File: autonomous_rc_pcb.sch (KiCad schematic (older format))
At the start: 19 parts, among them P1 USB_A_Vertical, P2 HDMI_PAUL, P7 USB_A_Vertical, U5 ESD-8040

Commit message: beta
beta pcb version 0.001V
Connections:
- net +12C: no longer ETHERNET1.6 (POE_VCC)
- net +28V: no longer POWER1.1 (Pin_1)
- new net +12V: ETHERNET1.6 (POE_VCC)
- new net +36V: POWER1.1 (Pin_1)
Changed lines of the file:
@@
-	1    0    0    -1
-$EndComp
-$Comp
-L +28V #PWR015
-U 1 1 5AF6179F
-P 1200 1350
-F 0 "#PWR015" H 1200 1200 50  0001 C CNN
-F 1 "+28V" H 1200 1500 50  0000 C CNN
-F 2 "" H 1450 1400 50  0001 C CNN
-F 3 "" H 1450 1400 50  0001 C CNN
-	1    1200 1350
 	1    0    0    -1
 $EndComp
@@
 	1    0    0    -1
 $EndComp
-$Comp
-L +12C #PWR039
-U 1 1 5B01DB59
-P 11550 6200
-F 0 "#PWR039" H 11550 6050 50  0001 C CNN
-F 1 "+12C" H 11550 6350 50  0000 C CNN
-F 2 "" H 11550 6200 50  0001 C CNN
-F 3 "" H 11550 6200 50  0001 C CNN
-	1    11550 6200
-	1    0    0    -1
-$EndComp
 NoConn ~ 11350 6150
 NoConn ~ 11350 6250
@@
 USB_ETHER+
 $Comp
-L GND #PWR040
+L GND #PWR039
 U 1 1 5B03A700
 P 10050 7450
-F 0 "#PWR040" H 10050 7200 50  0001 C CNN
+F 0 "#PWR039" H 10050 7200 50  0001 C CNN
 F 1 "GND" H 10050 7300 50  0000 C CNN
 F 2 "" H 10050 7450 50  0001 C CNN
@@
 $EndComp
 $Comp
-L GND #PWR041
+L GND #PWR040
 U 1 1 5B03A9DA
 P 10200 7450
-F 0 "#PWR041" H 10200 7200 50  0001 C CNN
+F 0 "#PWR040" H 10200 7200 50  0001 C CNN
 F 1 "GND" H 10200 7300 50  0000 C CNN
 F 2 "" H 10200 7450 50  0001 C CNN
@@
 Connection ~ 11850 3450
 Connection ~ 13050 3450
+$Comp
+L +12V #PWR041
+U 1 1 5B054AB8
+P 11550 6200
+F 0 "#PWR041" H 11550 6050 50  0001 C CNN
+F 1 "+12V" H 11550 6340 50  0000 C CNN
+F 2 "" H 11550 6200 50  0001 C CNN
+F 3 "" H 11550 6200 50  0001 C CNN
+	1    11550 6200
+	1    0    0    -1
+$EndComp
+$Comp
+L +36V #PWR?
+U 1 1 5B06C817
+P 1200 1350
+F 0 "#PWR?" H 1200 1200 50  0001 C CNN
+F 1 "+36V" H 1200 1490 50  0000 C CNN
+F 2 "" H 1200 1350 50  0001 C CNN
+F 3 "" H 1200 1350 50  0001 C CNN
+	1    1200 1350
+	1    0    0    -1
+$EndComp
 $EndSCHEMATC

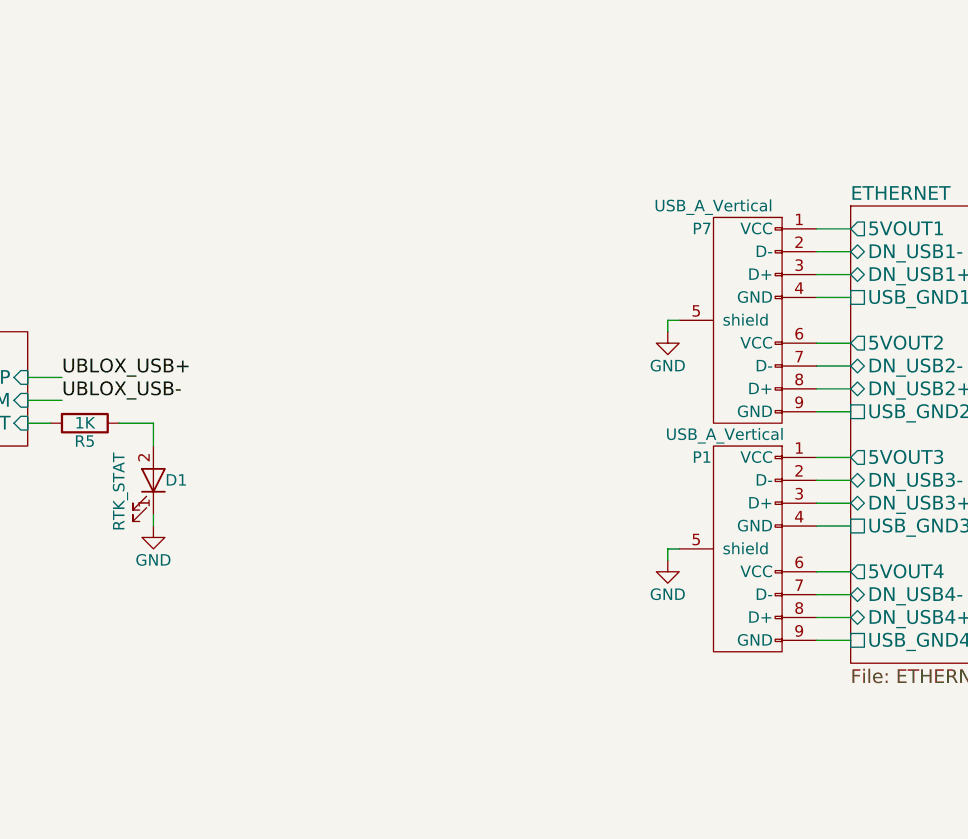
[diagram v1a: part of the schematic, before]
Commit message: tuned rf
added u.fl connectors to tune line 
moved some lines under rf components
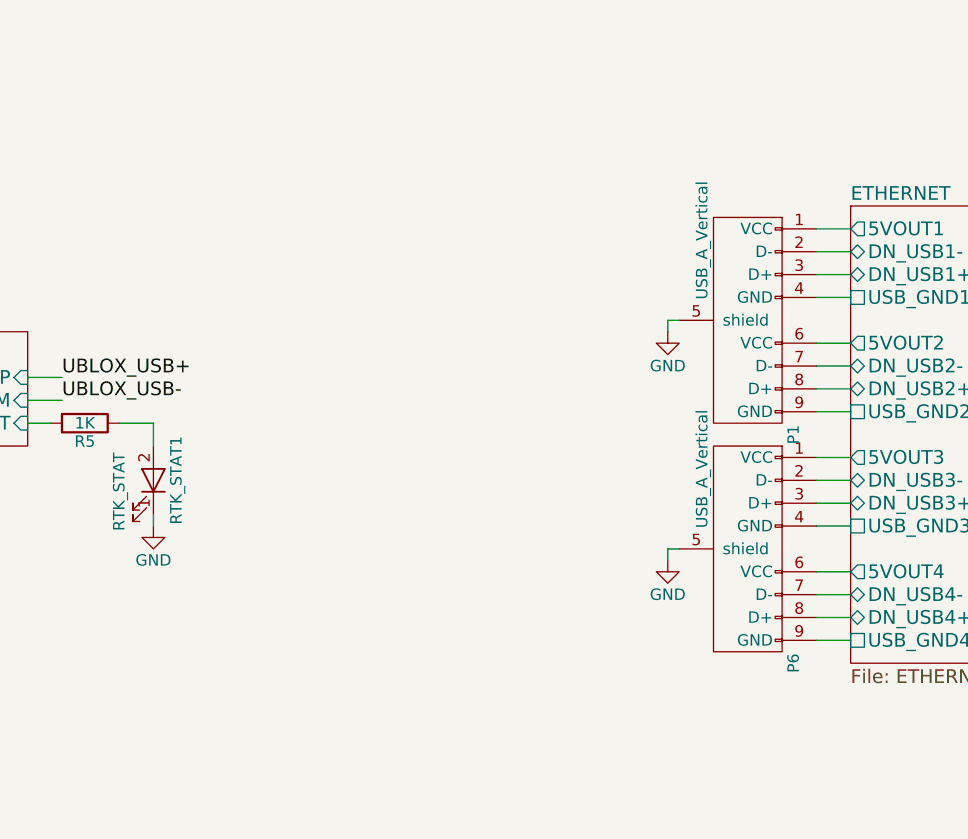
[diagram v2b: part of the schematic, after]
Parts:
- removed P7: USB_A_Vertical, Don-Con:USB_A_Stacked, symbol USB_A_Vertical
- added P6: USB_A_Vertical, Don-Con:USB-A-vertical, symbol USB_A_Vertical
- P1: footprint Don-Con:USB_A_Stacked -> Don-Con:USB-A-vertical
- renumbered D1 to RTK_STAT1
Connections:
- net ETHERNET/5VOUT1: now also P1.1 (VCC)
- net ETHERNET/5VOUT2: now also P1.6 (VCC)
- net ETHERNET/5VOUT3: now also P6.1 (VCC); no longer P1.1 (VCC)
- net ETHERNET/5VOUT4: now also P6.6 (VCC); no longer P1.6 (VCC)
- net ETHERNET/DN_USB1+: now also P1.3 (D+)
- net ETHERNET/DN_USB1-: now also P1.2 (D-)
- net ETHERNET/DN_USB2+: now also P1.8 (D+)
- net ETHERNET/DN_USB2-: now also P1.7 (D-)
- net ETHERNET/DN_USB3+: now also P6.3 (D+); no longer P1.3 (D+)
- net ETHERNET/DN_USB3-: now also P6.2 (D-); no longer P1.2 (D-)
- net ETHERNET/DN_USB4+: now also P6.8 (D+); no longer P1.8 (D+)
- net ETHERNET/DN_USB4-: now also P6.7 (D-); no longer P1.7 (D-)
- net ETHERNET/USB_GND1: now also P1.4 (GND)
- net ETHERNET/USB_GND2: now also P1.9 (GND)
- net ETHERNET/USB_GND3: now also P6.4 (GND); no longer P1.4 (GND)
- net ETHERNET/USB_GND4: now also P6.9 (GND); no longer P1.9 (GND)
- net GND: now also P6.5 (shield)
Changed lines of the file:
@@
 $EndSheet
 $Comp
-L LED D1
+L LED RTK_STAT1
 U 1 1 5AF2A043
 P 5300 6250
-F 0 "D1" V 5300 6350 50  0000 C CNN
+F 0 "RTK_STAT1" H 5300 6350 50  0000 C CNN
 F 1 "RTK_STAT" H 5250 6100 50  0000 C CNN
 F 2 "LEDs:LED_0603" H 5300 6250 50  0001 C CNN
@@
 STM_USB_N
 $Comp
-L +28V #PWR016
+L +28V #PWR015
 U 1 1 5AF68A51
 P 3100 900
-F 0 "#PWR016" H 3100 750 50  0001 C CNN
+F 0 "#PWR015" H 3100 750 50  0001 C CNN
 F 1 "+28V" H 3100 1050 50  0000 C CNN
 F 2 "" H 3350 950 50  0001 C CNN
@@
 $EndComp
 $Comp
-L +3V3 #PWR017
+L +3V3 #PWR016
 U 1 1 5AF68C87
 P 3900 900
-F 0 "#PWR017" H 3900 750 50  0001 C CNN
+F 0 "#PWR016" H 3900 750 50  0001 C CNN
 F 1 "+3V3" H 3900 1040 50  0000 C CNN
 F 2 "" H 3900 900 50  0001 C CNN
@@
 $EndComp
 $Comp
-L +1V8 #PWR018
+L +1V8 #PWR017
 U 1 1 5AF68EBD
 P 4300 900
-F 0 "#PWR018" H 4300 750 50  0001 C CNN
+F 0 "#PWR017" H 4300 750 50  0001 C CNN
 F 1 "+1V8" H 4300 1040 50  0000 C CNN
 F 2 "" H 4300 900 50  0001 C CNN
@@
 $EndComp
 $Comp
-L +5V #PWR019
+L +5V #PWR018
 U 1 1 5AF690F3
 P 4700 900
-F 0 "#PWR019" H 4700 750 50  0001 C CNN
+F 0 "#PWR018" H 4700 750 50  0001 C CNN
 F 1 "+5V" H 4700 1040 50  0000 C CNN
 F 2 "" H 4700 900 50  0001 C CNN
@@
 $EndComp
 $Comp
-L GND #PWR020
+L GND #PWR019
 U 1 1 5AF69329
 P 5000 1150
-F 0 "#PWR020" H 5000 900 50  0001 C CNN
+F 0 "#PWR019" H 5000 900 50  0001 C CNN
 F 1 "GND" H 5000 1000 50  0000 C CNN
 F 2 "" H 5000 1150 50  0001 C CNN
@@
 $EndComp
 $Comp
-L PWR_FLAG #FLG021
+L PWR_FLAG #FLG020
 U 1 1 5AF6955F
 P 5000 900
-F 0 "#FLG021" H 5000 975 50  0001 C CNN
+F 0 "#FLG020" H 5000 975 50  0001 C CNN
 F 1 "PWR_FLAG" H 5000 1050 50  0000 C CNN
 F 2 "" H 5000 900 50  0001 C CNN
@@
 $EndComp
 $Comp
-L PWR_FLAG #FLG022
+L PWR_FLAG #FLG021
 U 1 1 5AF69795
 P 3100 1150
-F 0 "#FLG022" H 3100 1225 50  0001 C CNN
+F 0 "#FLG021" H 3100 1225 50  0001 C CNN
 F 1 "PWR_FLAG" H 3100 1300 50  0000 C CNN
 F 2 "" H 3100 1150 50  0001 C CNN
@@
 $EndComp
 $Comp
-L PWR_FLAG #FLG023
+L PWR_FLAG #FLG022
 U 1 1 5AF69BF4
 P 3900 1150
-F 0 "#FLG023" H 3900 1225 50  0001 C CNN
+F 0 "#FLG022" H 3900 1225 50  0001 C CNN
 F 1 "PWR_FLAG" H 3900 1300 50  0000 C CNN
 F 2 "" H 3900 1150 50  0001 C CNN
@@
 $EndComp
 $Comp
-L PWR_FLAG #FLG024
+L PWR_FLAG #FLG023
 U 1 1 5AF69E2A
 P 4300 1150
-F 0 "#FLG024" H 4300 1225 50  0001 C CNN
+F 0 "#FLG023" H 4300 1225 50  0001 C CNN
 F 1 "PWR_FLAG" H 4300 1300 50  0000 C CNN
 F 2 "" H 4300 1150 50  0001 C CNN
@@
 $EndComp
 $Comp
-L PWR_FLAG #FLG025
+L PWR_FLAG #FLG024
 U 1 1 5AF6A060
 P 4700 1150
-F 0 "#FLG025" H 4700 1225 50  0001 C CNN
+F 0 "#FLG024" H 4700 1225 50  0001 C CNN
 F 1 "PWR_FLAG" H 4700 1300 50  0000 C CNN
 F 2 "" H 4700 1150 50  0001 C CNN
@@
 NoConn ~ 11850 3250
 $Comp
-L +5V #PWR026
+L +5V #PWR025
 U 1 1 5AF9117D
 P 13200 3650
-F 0 "#PWR026" H 13200 3500 50  0001 C CNN
+F 0 "#PWR025" H 13200 3500 50  0001 C CNN
 F 1 "+5V" H 13200 3790 50  0000 C CNN
 F 2 "" H 13200 3650 50  0001 C CNN
@@
 UBLOX_USB-
 $Comp
-L +5V #PWR027
+L +5V #PWR026
 U 1 1 5AFDF0D4
 P 1500 7350
-F 0 "#PWR027" H 1500 7200 50  0001 C CNN
+F 0 "#PWR026" H 1500 7200 50  0001 C CNN
 F 1 "+5V" H 1500 7490 50  0000 C CNN
 F 2 "" H 1500 7350 50  0001 C CNN
@@
 $EndComp
 $Comp
-L GND #PWR028
+L GND #PWR027
 U 1 1 5AFDF0DA
 P 1650 7650
-F 0 "#PWR028" H 1650 7400 50  0001 C CNN
+F 0 "#PWR027" H 1650 7400 50  0001 C CNN
 F 1 "GND" H 1650 7500 50  0000 C CNN
 F 2 "" H 1650 7650 50  0001 C CNN
@@
 $EndComp
 $Comp
-L +5V #PWR029
+L +5V #PWR028
 U 1 1 5AFDF99D
 P 1500 8000
-F 0 "#PWR029" H 1500 7850 50  0001 C CNN
+F 0 "#PWR028" H 1500 7850 50  0001 C CNN
 F 1 "+5V" H 1500 8140 50  0000 C CNN
 F 2 "" H 1500 8000 50  0001 C CNN
@@
 $EndComp
 $Comp
-L GND #PWR030
+L GND #PWR029
 U 1 1 5AFDF9A3
 P 1650 8300
-F 0 "#PWR030" H 1650 8050 50  0001 C CNN
+F 0 "#PWR029" H 1650 8050 50  0001 C CNN
 F 1 "GND" H 1650 8150 50  0000 C CNN
 F 2 "" H 1650 8300 50  0001 C CNN
@@
 $EndComp
 $Comp
-L +5V #PWR031
+L +5V #PWR030
 U 1 1 5AFDFFC7
 P 1500 8650
-F 0 "#PWR031" H 1500 8500 50  0001 C CNN
+F 0 "#PWR030" H 1500 8500 50  0001 C CNN
 F 1 "+5V" H 1500 8790 50  0000 C CNN
 F 2 "" H 1500 8650 50  0001 C CNN
@@
 $EndComp
 $Comp
-L GND #PWR032
+L GND #PWR031
 U 1 1 5AFDFFCD
 P 1650 8950
-F 0 "#PWR032" H 1650 8700 50  0001 C CNN
+F 0 "#PWR031" H 1650 8700 50  0001 C CNN
 F 1 "GND" H 1650 8800 50  0000 C CNN
 F 2 "" H 1650 8950 50  0001 C CNN
@@
 VBAT_ADC
 $Comp
-L PWR_FLAG #FLG033
+L PWR_FLAG #FLG032
 U 1 1 5B0318FE
 P 3500 1150
-F 0 "#FLG033" H 3500 1225 50  0001 C CNN
+F 0 "#FLG032" H 3500 1225 50  0001 C CNN
 F 1 "PWR_FLAG" H 3500 1300 50  0000 C CNN
 F 2 "" H 3500 1150 50  0001 C CNN
@@
 $EndComp
 $Comp
-L +12C #PWR034
+L +12C #PWR033
 U 1 1 5B031F00
 P 3500 900
-F 0 "#PWR034" H 3500 750 50  0001 C CNN
+F 0 "#PWR033" H 3500 750 50  0001 C CNN
 F 1 "+12C" H 3500 1050 50  0000 C CNN
 F 2 "" H 3500 900 50  0001 C CNN
@@
 UBLOX_USB-
 $Comp
-L GND #PWR035
+L GND #PWR034
 U 1 1 5AFCCFA1
 P 7550 5600
-F 0 "#PWR035" H 7550 5350 50  0001 C CNN
+F 0 "#PWR034" H 7550 5350 50  0001 C CNN
 F 1 "GND" H 7550 5450 50  0000 C CNN
 F 2 "" H 7550 5600 50  0001 C CNN
 F 3 "" H 7550 5600 50  0001 C CNN
 	1    7550 5600
-	1    0    0    -1
-$EndComp
-$Comp
-L USB_A_Vertical P7
-U 1 1 5AFCCF9B
-P 8000 5550
-F 0 "P7" H 7700 5950 50  0000 C CNN
-F 1 "USB_A_Vertical" H 7750 6050 50  0000 C CNN
-F 2 "Don-Con:USB_A_Stacked" H 8000 5300 60  0001 C CNN
-F 3 "" H 8000 5300 60  0000 C CNN
-	1    8000 5550
 	1    0    0    -1
 $EndComp
@@
 $EndSheet
 $Comp
-L GND #PWR036
+L GND #PWR035
 U 1 1 5B006ACE
 P 7550 6600
-F 0 "#PWR036" H 7550 6350 50  0001 C CNN
+F 0 "#PWR035" H 7550 6350 50  0001 C CNN
 F 1 "GND" H 7550 6450 50  0000 C CNN
 F 2 "" H 7550 6600 50  0001 C CNN
 F 3 "" H 7550 6600 50  0001 C CNN
 	1    7550 6600
-	1    0    0    -1
-$EndComp
-$Comp
-L USB_A_Vertical P1
-U 1 1 5B006AD4
-P 8000 6550
-F 0 "P1" H 7700 6950 50  0000 C CNN
-F 1 "USB_A_Vertical" H 7800 7050 50  0000 C CNN
-F 2 "Don-Con:USB_A_Stacked" H 8000 6300 60  0001 C CNN
-F 3 "" H 8000 6300 60  0000 C CNN
-	1    8000 6550
 	1    0    0    -1
 $EndComp
@@
 $EndComp
 $Comp
-L GND #PWR037
+L GND #PWR036
 U 1 1 5B01D54D
 P 11450 7050
-F 0 "#PWR037" H 11450 6800 50  0001 C CNN
+F 0 "#PWR036" H 11450 6800 50  0001 C CNN
 F 1 "GND" H 11450 6900 50  0000 C CNN
 F 2 "" H 11450 7050 50  0001 C CNN
@@
 $EndComp
 $Comp
-L GND #PWR038
+L GND #PWR037
 U 1 1 5B01D853
 P 11450 6550
-F 0 "#PWR038" H 11450 6300 50  0001 C CNN
+F 0 "#PWR037" H 11450 6300 50  0001 C CNN
 F 1 "GND" H 11450 6400 50  0000 C CNN
 F 2 "" H 11450 6550 50  0001 C CNN
@@
 USB_ETHER+
 $Comp
-L GND #PWR039
+L GND #PWR038
 U 1 1 5B03A700
 P 10050 7450
-F 0 "#PWR039" H 10050 7200 50  0001 C CNN
+F 0 "#PWR038" H 10050 7200 50  0001 C CNN
 F 1 "GND" H 10050 7300 50  0000 C CNN
 F 2 "" H 10050 7450 50  0001 C CNN
@@
 $EndComp
 $Comp
-L GND #PWR040
+L GND #PWR039
 U 1 1 5B03A9DA
 P 10200 7450
-F 0 "#PWR040" H 10200 7200 50  0001 C CNN
+F 0 "#PWR039" H 10200 7200 50  0001 C CNN
 F 1 "GND" H 10200 7300 50  0000 C CNN
 F 2 "" H 10200 7450 50  0001 C CNN
@@
 Connection ~ 13050 3450
 $Comp
-L +12V #PWR041
+L +12V #PWR040
 U 1 1 5B054AB8
 P 11550 6200
-F 0 "#PWR041" H 11550 6050 50  0001 C CNN
+F 0 "#PWR040" H 11550 6050 50  0001 C CNN
 F 1 "+12V" H 11550 6340 50  0000 C CNN
 F 2 "" H 11550 6200 50  0001 C CNN
@@
 $EndComp
 $Comp
-L +36V #PWR?
+L +36V #PWR041
 U 1 1 5B06C817
 P 1200 1350
-F 0 "#PWR?" H 1200 1200 50  0001 C CNN
+F 0 "#PWR041" H 1200 1200 50  0001 C CNN
 F 1 "+36V" H 1200 1490 50  0000 C CNN
 F 2 "" H 1200 1350 50  0001 C CNN
@@
 	1    0    0    -1
 $EndComp
+$Comp
+L USB_A_Vertical P1
+U 1 1 5B085B2E
+P 8000 5550
+F 0 "P1" V 8100 5050 50  0000 C CNN
+F 1 "USB_A_Vertical" V 7700 5900 50  0000 C CNN
+F 2 "Don-Con:USB-A-vertical" H 7950 4900 60  0001 C CNN
+F 3 "" H 8000 5300 60  0000 C CNN
+	1    8000 5550
+	1    0    0    -1
+$EndComp
+$Comp
+L USB_A_Vertical P6
+U 1 1 5B085E47
+P 8000 6550
+F 0 "P6" V 8100 6050 50  0000 C CNN
+F 1 "USB_A_Vertical" V 7700 6900 50  0000 C CNN
+F 2 "Don-Con:USB-A-vertical" H 7950 5900 60  0001 C CNN
+F 3 "" H 8000 6300 60  0000 C CNN
+	1    8000 6550
+	1    0    0    -1
+$EndComp
